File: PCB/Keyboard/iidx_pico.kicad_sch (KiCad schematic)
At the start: 79 parts, among them J1 Spin, J2 Spin, J3 RGB, J4 RGB, J5 Spin, J6 Spin, SW1 SWITCH_SPST, SW10 SWITCH_SPST, SW11 SWITCH_SPST, SW12 Tact_4pin, SW13 Tact_4pin, SW2 SWITCH_SPST, SW3 SWITCH_SPST, SW4 SWITCH_SPST, SW5 SWITCH_SPST, SW6 SWITCH_SPST, SW7 SWITCH_SPST, SW8 SWITCH_SPST, SW9 SWITCH_SPST, U1 PiPico_No_SWD, U2 TMAG5273, U3 AS5600

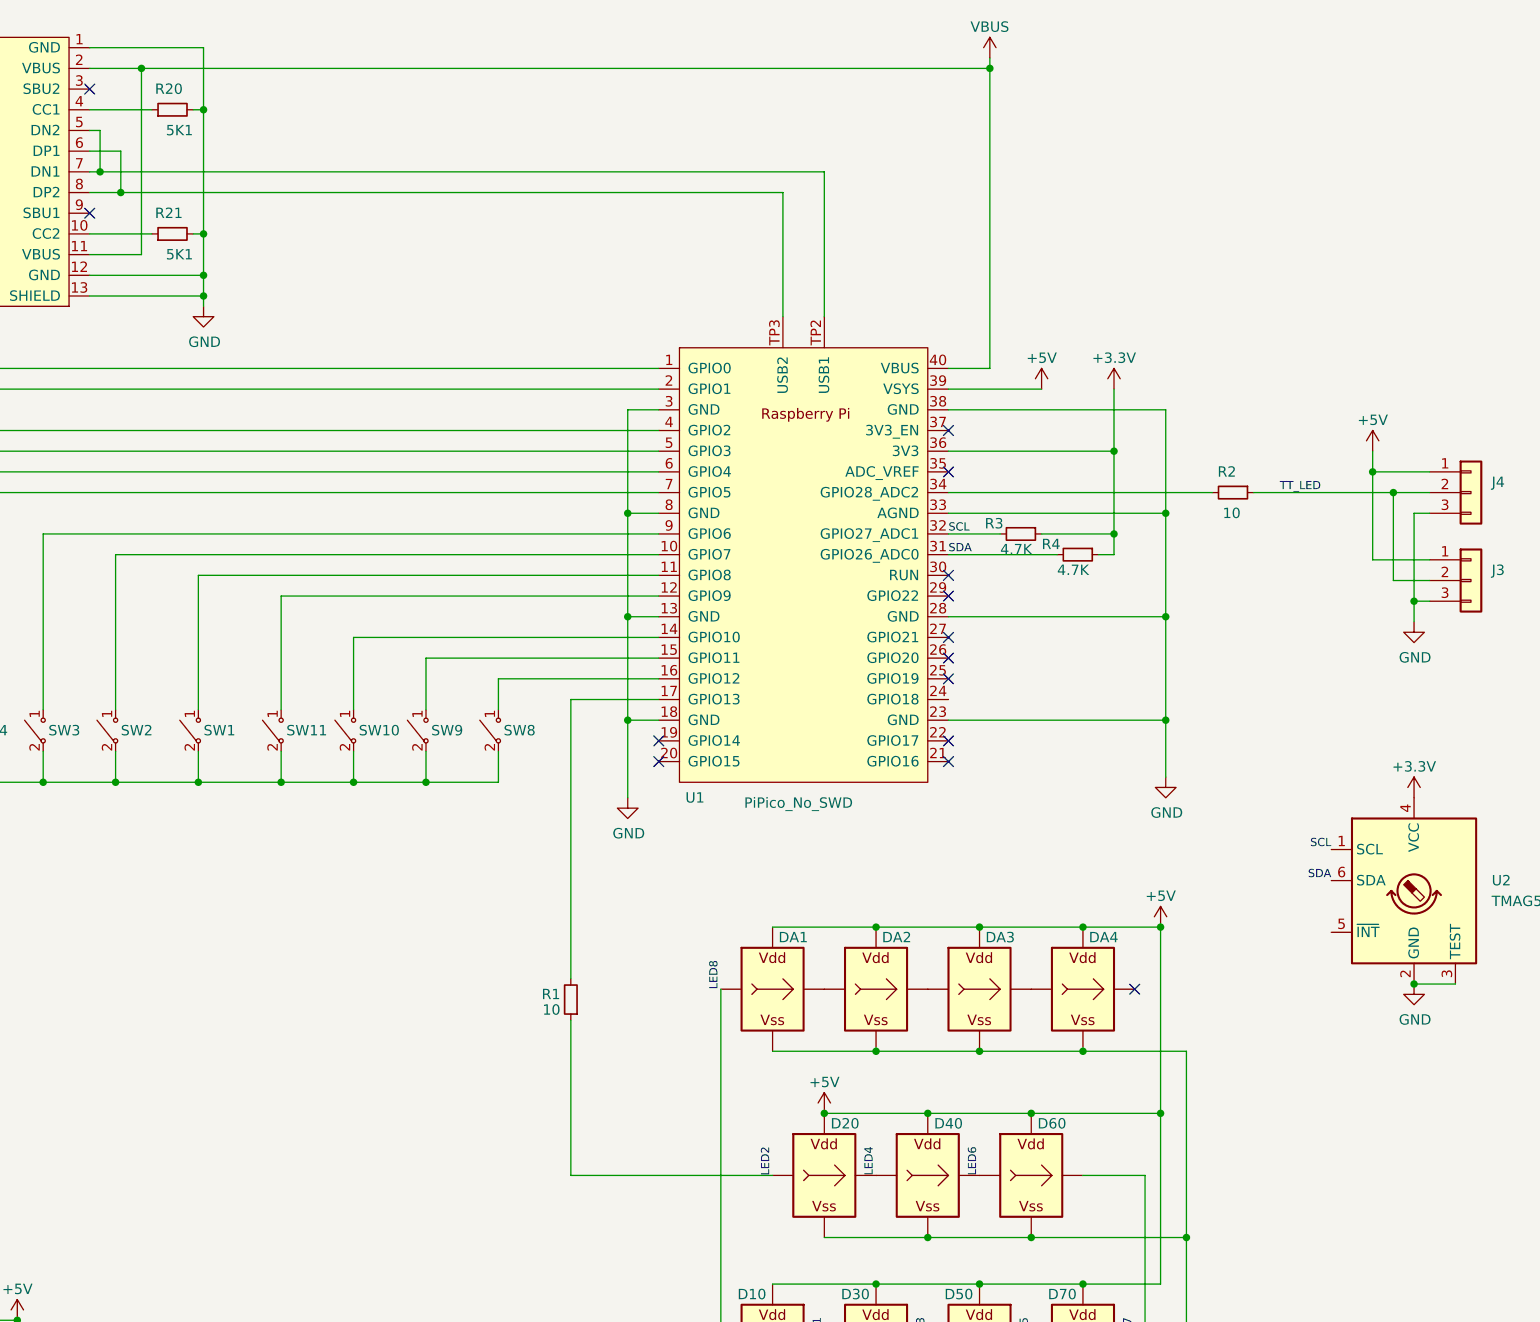
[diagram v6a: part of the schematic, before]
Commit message: PCB v1.41 (better 1615 LED footprint)
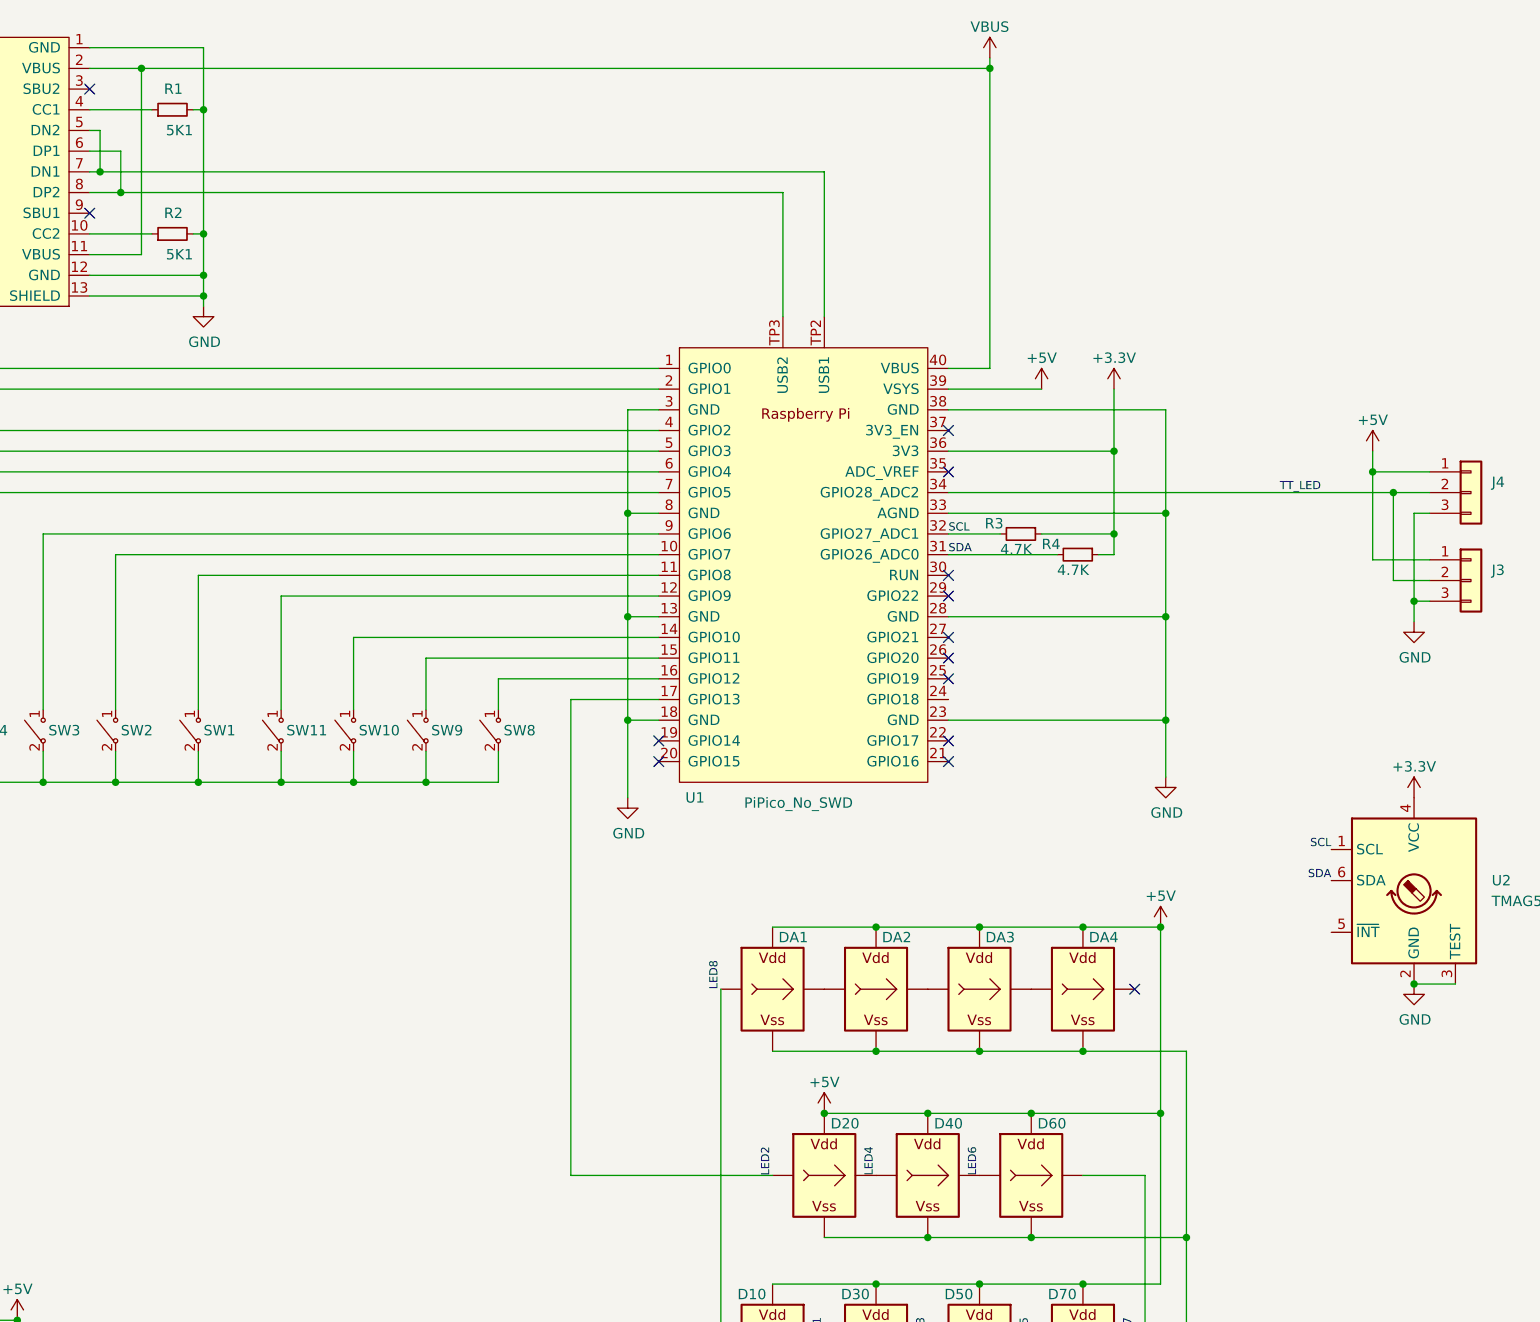
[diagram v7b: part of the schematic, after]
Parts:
- removed R1, R2: 10, Resistor_SMD:R_0603_1608Metric_Pad0.98x0.95mm_HandSolder, symbol Device:R_Small
- renumbered R20 to R1, R21 to R2
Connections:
- net LED2: now also U1.17 (GPIO13)
- net TT_LED: now also U1.34 (GPIO28_ADC2)
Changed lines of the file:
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@@
 	(wire
 		(pts
-			(xy 231.775 81.28) (xy 264.16 81.28)
+			(xy 231.775 81.28) (xy 286.385 81.28)
 		)
 		(stroke
@@
 	(wire
 		(pts
-			(xy 185.42 146.05) (xy 185.42 165.1)
+			(xy 185.42 106.68) (xy 185.42 165.1)
 		)
 		(stroke
@@
 	(wire
 		(pts
-			(xy 269.24 81.28) (xy 286.385 81.28)
-		)
-		(stroke
-			(width 0)
-			(type default)
-		)
-	)
-	(wire
-		(pts
 			(xy 235.585 178.435) (xy 248.285 178.435)
 		)
@@
 	(wire
 		(pts
-			(xy 185.42 106.68) (xy 185.42 140.97)
-		)
-		(stroke
-			(width 0)
-			(type default)
-		)
-	)
-	(wire
-		(pts
 			(xy 80.645 240.03) (xy 80.645 251.46)
 		)
@@
 		(on_board yes)
 		(dnp no)
-		(property "Reference" "R21"
+		(property "Reference" "R2"
 			(at 137.795 46.99 90)
 			(effects
@@
 			(project "iidx_pico"
 				(path "/2e3f5573-c264-4a8b-a2f0-0e6473d39aad"
-					(reference "R21")
+					(reference "R2")
 					(unit 1)
 				)
@@
 		(on_board yes)
 		(dnp no)
-		(property "Reference" "R20"
+		(property "Reference" "R1"
 			(at 137.795 31.75 90)
 			(effects
@@
 			(project "iidx_pico"
 				(path "/2e3f5573-c264-4a8b-a2f0-0e6473d39aad"
-					(reference "R20")
-					(unit 1)
-				)
-			)
-		)
-	)
-	(symbol
-		(lib_id "Device:R_Small")
-		(at 185.42 143.51 180)
-		(unit 1)
-		(exclude_from_sim no)
-		(in_bom yes)
-		(on_board yes)
-		(dnp no)
-		(property "Reference" "R1"
-			(at 184.15 142.875 0)
-			(effects
-				(font
-					(size 1.27 1.27)
-				)
-				(justify left)
-			)
-		)
-		(property "Value" "10"
-			(at 184.15 144.78 0)
-			(effects
-				(font
-					(size 1.27 1.27)
-				)
-				(justify left)
-			)
-		)
-		(property "Footprint" "Resistor_SMD:R_0603_1608Metric_Pad0.98x0.95mm_HandSolder"
-			(at 185.42 143.51 0)
-			(effects
-				(font
-					(size 1.27 1.27)
-				)
-				(hide yes)
-			)
-		)
-		(property "Datasheet" "~"
-			(at 185.42 143.51 0)
-			(effects
-				(font
-					(size 1.27 1.27)
-				)
-				(hide yes)
-			)
-		)
-		(property "Description" ""
-			(at 185.42 143.51 0)
-			(effects
-				(font
-					(size 1.27 1.27)
-				)
-				(hide yes)
-			)
-		)
-		(property "LCSC" "C23186"
-			(at 185.42 143.51 0)
-			(effects
-				(font
-					(size 1.27 1.27)
-				)
-				(hide yes)
-			)
-		)
-		(pin "1"
-		)
-		(pin "2"
-		)
-		(instances
-			(project "iidx_pico"
-				(path "/2e3f5573-c264-4a8b-a2f0-0e6473d39aad"
 					(reference "R1")
 					(unit 1)
@@
 					(unit 1)
 				)
-			)
-		)
-	)
-	(symbol
-		(lib_id "Device:R_Small")
-		(at 266.7 81.28 270)
-		(unit 1)
-		(exclude_from_sim no)
-		(in_bom yes)
-		(on_board yes)
-		(dnp no)
-		(property "Reference" "R2"
-			(at 264.795 78.74 90)
-			(effects
-				(font
-					(size 1.27 1.27)
-				)
-				(justify left)
-			)
-		)
-		(property "Value" "10"
-			(at 265.43 83.82 90)
-			(effects
-				(font
-					(size 1.27 1.27)
-				)
-				(justify left)
-			)
-		)
-		(property "Footprint" "Resistor_SMD:R_0603_1608Metric_Pad0.98x0.95mm_HandSolder"
-			(at 266.7 81.28 0)
-			(effects
-				(font
-					(size 1.27 1.27)
-				)
-				(hide yes)
-			)
-		)
-		(property "Datasheet" "~"
-			(at 266.7 81.28 0)
-			(effects
-				(font
-					(size 1.27 1.27)
-				)
-				(hide yes)
-			)
-		)
-		(property "Description" ""
-			(at 266.7 81.28 0)
-			(effects
-				(font
-					(size 1.27 1.27)
-				)
-				(hide yes)
-			)
-		)
-		(property "LCSC" "C23186"
-			(at 266.7 81.28 0)
-			(effects
-				(font
-					(size 1.27 1.27)
-				)
-				(hide yes)
-			)
-		)
-		(pin "1"
-		)
-		(pin "2"
-		)
-		(instances
-			(project "iidx_pico"
-				(path "/2e3f5573-c264-4a8b-a2f0-0e6473d39aad"
-					(reference "R2")
-					(unit 1)
-				)
